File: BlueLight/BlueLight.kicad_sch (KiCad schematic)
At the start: 9 parts, among them J1 Rotary Encoder, J2 LED, SW1 SW_Push_Dual, SW2 SW_Push_Dual, SW3 SW_Push_Dual

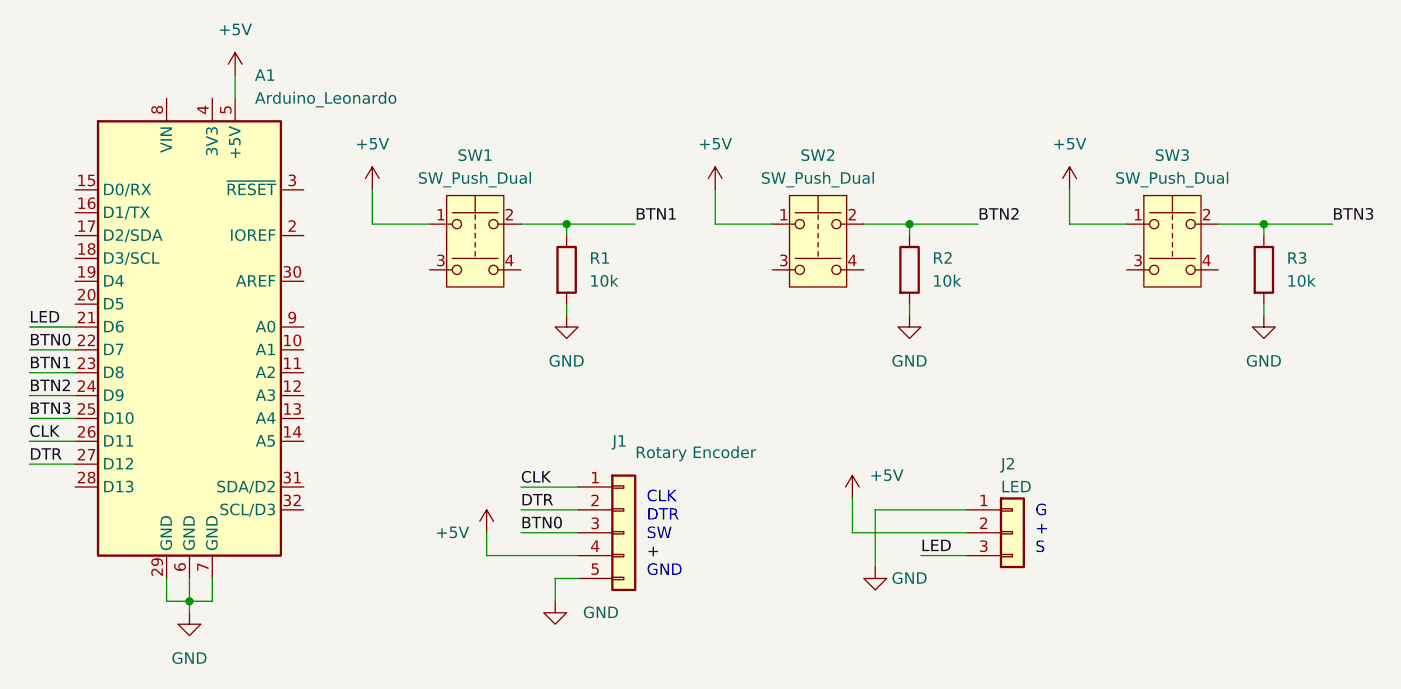
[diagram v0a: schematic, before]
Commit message: new app
timer added
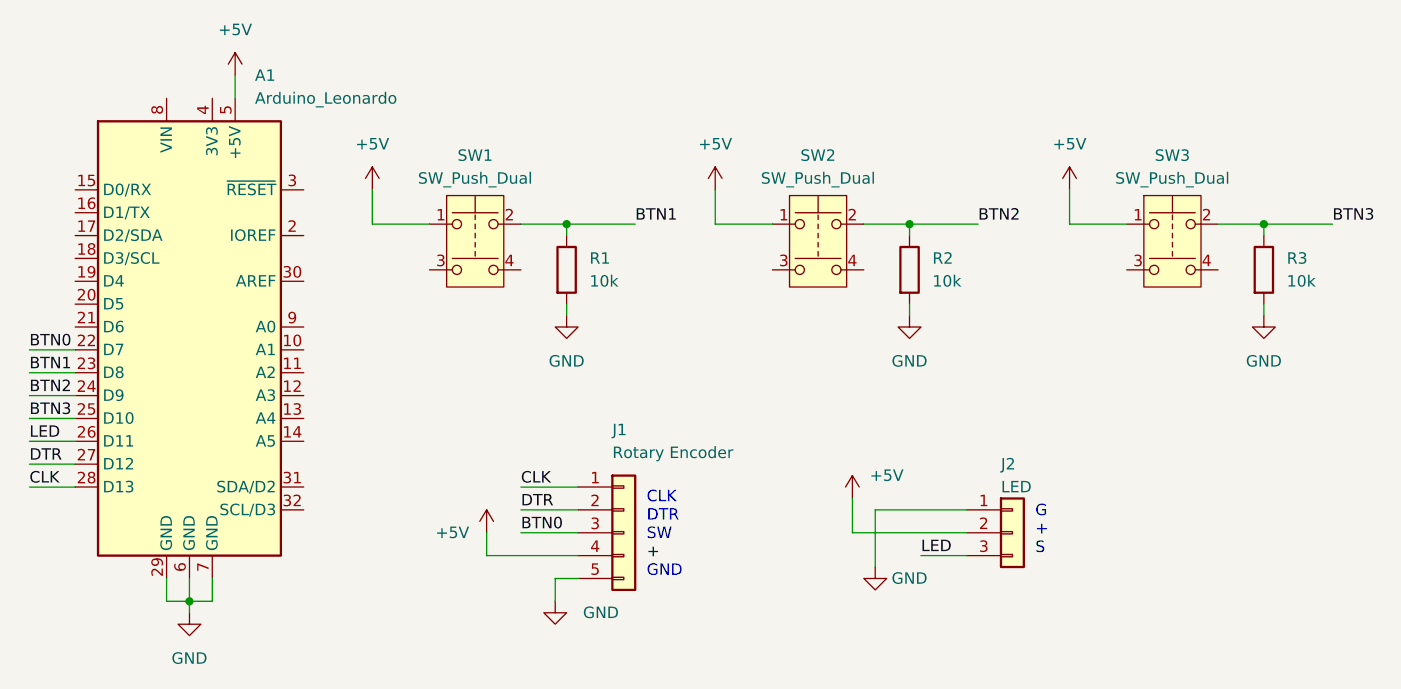
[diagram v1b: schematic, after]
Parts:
- A1: footprint Module:Arduino_UNO_R3 -> Module:Arduino_UNO_R3_WithMountingHoles
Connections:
- net CLK: now also A1.28 (D13); no longer A1.26 (D11)
- net LED: now also A1.26 (D11); no longer A1.21 (D6)
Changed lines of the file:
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@@
+    (stroke (width 0) (type default))
+  )
+  (wire (pts (xy 17.78 69.85) (xy 22.86 69.85))
     (stroke (width 0) (type default))
   )
@@
     (stroke (width 0) (type default))
   )
-  (wire (pts (xy 17.78 52.07) (xy 22.86 52.07))
-    (stroke (width 0) (type default))
-  )
   (wire (pts (xy 77.47 49.53) (xy 77.47 50.8))
     (stroke (width 0) (type default))
@@
     (effects (font (size 1.27 1.27)) (justify left bottom))
   )
-  (label "CLK" (at 17.78 64.77 0) (fields_autoplaced)
+  (label "CLK" (at 17.78 69.85 0) (fields_autoplaced)
     (effects (font (size 1.27 1.27)) (justify left bottom))
   )
@@
     (effects (font (size 1.27 1.27)) (justify left bottom))
   )
-  (label "LED" (at 17.78 52.07 0) (fields_autoplaced)
+  (label "LED" (at 17.78 64.77 0) (fields_autoplaced)
     (effects (font (size 1.27 1.27)) (justify left bottom))
   )
@@
   (symbol (lib_id "Connector_Generic:Conn_01x05") (at 83.82 74.93 0) (unit 1)
     (in_bom yes) (on_board yes) (dnp no)
-    (property "Reference" "J1" (at 82.55 64.77 0)
-      (effects (font (size 1.27 1.27)) (justify left))
-    )
-    (property "Value" "Rotary Encoder" (at 85.09 66.04 0)
+    (property "Reference" "J1" (at 82.55 63.5 0)
+      (effects (font (size 1.27 1.27)) (justify left))
+    )
+    (property "Value" "Rotary Encoder" (at 82.55 66.04 0)
       (effects (font (size 1.27 1.27)) (justify left))
     )
@@
       (effects (font (size 1.27 1.27)) (justify left))
     )
-    (property "Footprint" "Module:Arduino_UNO_R3" (at 35.56 52.07 0)
+    (property "Footprint" "Module:Arduino_UNO_R3_WithMountingHoles" (at 35.56 52.07 0)
       (effects (font (size 1.27 1.27) italic) hide)
     )

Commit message: doule version init
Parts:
- added J3: LED, Connector_PinHeader_2.54mm:PinHeader_1x03_P2.54mm_Vertical, symbol Connector_Generic:Conn_01x03
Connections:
- net +5V: now also J3.2 (Pin_2)
- net GND: now also J3.1 (Pin_1)
- net LED_2: now reaches A1.18 (D3/SCL)
- net LED_2: now also J3.3 (Pin_3)
- net LED renamed LED_1
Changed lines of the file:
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@@
+    (stroke (width 0) (type default))
+  )
+  (wire (pts (xy 144.78 71.12) (xy 144.78 74.93))
     (stroke (width 0) (type default))
   )
@@
     (stroke (width 0) (type default))
   )
-  (wire (pts (xy 17.78 57.15) (xy 22.86 57.15))
+  (wire (pts (xy 16.51 57.15) (xy 22.86 57.15))
     (stroke (width 0) (type default))
   )
@@
     (stroke (width 0) (type default))
   )
-  (wire (pts (xy 17.78 64.77) (xy 22.86 64.77))
+  (wire (pts (xy 16.51 64.77) (xy 22.86 64.77))
     (stroke (width 0) (type default))
   )
@@
     (stroke (width 0) (type default))
   )
+  (wire (pts (xy 16.51 44.45) (xy 22.86 44.45))
+    (stroke (width 0) (type default))
+  )
   (wire (pts (xy 115.57 40.64) (xy 123.19 40.64))
     (stroke (width 0) (type default))
   )
-  (wire (pts (xy 17.78 67.31) (xy 22.86 67.31))
+  (wire (pts (xy 16.51 67.31) (xy 22.86 67.31))
     (stroke (width 0) (type default))
   )
@@
     (stroke (width 0) (type default))
   )
-  (wire (pts (xy 17.78 69.85) (xy 22.86 69.85))
+  (wire (pts (xy 16.51 54.61) (xy 22.86 54.61))
+    (stroke (width 0) (type default))
+  )
+  (wire (pts (xy 16.51 69.85) (xy 22.86 69.85))
     (stroke (width 0) (type default))
   )
@@
     (stroke (width 0) (type default))
   )
-  (wire (pts (xy 17.78 62.23) (xy 22.86 62.23))
-    (stroke (width 0) (type default))
-  )
   (wire (pts (xy 35.56 80.01) (xy 35.56 82.55))
     (stroke (width 0) (type default))
@@
     (stroke (width 0) (type default))
   )
+  (wire (pts (xy 152.4 77.47) (xy 157.48 77.47))
+    (stroke (width 0) (type default))
+  )
+  (wire (pts (xy 147.32 72.39) (xy 147.32 78.74))
+    (stroke (width 0) (type default))
+  )
   (wire (pts (xy 111.76 72.39) (xy 111.76 78.74))
     (stroke (width 0) (type default))
@@
     (stroke (width 0) (type default))
   )
+  (wire (pts (xy 147.32 72.39) (xy 157.48 72.39))
+    (stroke (width 0) (type default))
+  )
   (wire (pts (xy 77.47 49.53) (xy 77.47 50.8))
     (stroke (width 0) (type default))
   )
+  (wire (pts (xy 16.51 59.69) (xy 22.86 59.69))
+    (stroke (width 0) (type default))
+  )
+  (wire (pts (xy 16.51 62.23) (xy 22.86 62.23))
+    (stroke (width 0) (type default))
+  )
   (wire (pts (xy 111.76 72.39) (xy 121.92 72.39))
     (stroke (width 0) (type default))
   )
-  (wire (pts (xy 17.78 59.69) (xy 22.86 59.69))
-    (stroke (width 0) (type default))
-  )
   (wire (pts (xy 154.94 40.64) (xy 162.56 40.64))
     (stroke (width 0) (type default))
@@
     (stroke (width 0) (type default))
   )
-  (wire (pts (xy 17.78 54.61) (xy 22.86 54.61))
-    (stroke (width 0) (type default))
-  )
   (wire (pts (xy 38.1 82.55) (xy 38.1 80.01))
     (stroke (width 0) (type default))
   )
+  (wire (pts (xy 144.78 74.93) (xy 157.48 74.93))
+    (stroke (width 0) (type default))
+  )
+  (text "G\n+\nS" (at 165.1 77.47 0)
+    (effects (font (size 1.27 1.27)) (justify left bottom))
+  )
   (text "G\n+\nS" (at 129.54 77.47 0)
     (effects (font (size 1.27 1.27)) (justify left bottom))
@@
     (effects (font (size 1.27 1.27)) (justify left bottom))
   )
-  (label "DTR" (at 17.78 67.31 0) (fields_autoplaced)
-    (effects (font (size 1.27 1.27)) (justify left bottom))
-  )
-  (label "CLK" (at 17.78 69.85 0) (fields_autoplaced)
+  (label "DTR" (at 16.51 67.31 0) (fields_autoplaced)
+    (effects (font (size 1.27 1.27)) (justify left bottom))
+  )
+  (label "CLK" (at 16.51 69.85 0) (fields_autoplaced)
     (effects (font (size 1.27 1.27)) (justify left bottom))
   )
@@
     (effects (font (size 1.27 1.27)) (justify left bottom))
   )
-  (label "BTN2" (at 17.78 59.69 0) (fields_autoplaced)
-    (effects (font (size 1.27 1.27)) (justify left bottom))
-  )
-  (label "LED" (at 116.84 77.47 0) (fields_autoplaced)
+  (label "BTN2" (at 16.51 59.69 0) (fields_autoplaced)
+    (effects (font (size 1.27 1.27)) (justify left bottom))
+  )
+  (label "LED_1" (at 116.84 77.47 0) (fields_autoplaced)
     (effects (font (size 1.27 1.27)) (justify left bottom))
   )
@@
     (effects (font (size 1.27 1.27)) (justify left bottom))
   )
-  (label "BTN3" (at 17.78 62.23 0) (fields_autoplaced)
+  (label "LED_2" (at 16.51 44.45 0) (fields_autoplaced)
+    (effects (font (size 1.27 1.27)) (justify left bottom))
+  )
+  (label "BTN3" (at 16.51 62.23 0) (fields_autoplaced)
+    (effects (font (size 1.27 1.27)) (justify left bottom))
+  )
+  (label "LED_2" (at 152.4 77.47 0) (fields_autoplaced)
     (effects (font (size 1.27 1.27)) (justify left bottom))
   )
@@
     (effects (font (size 1.27 1.27)) (justify left bottom))
   )
-  (label "BTN1" (at 17.78 57.15 0) (fields_autoplaced)
-    (effects (font (size 1.27 1.27)) (justify left bottom))
-  )
-  (label "LED" (at 17.78 64.77 0) (fields_autoplaced)
+  (label "BTN1" (at 16.51 57.15 0) (fields_autoplaced)
+    (effects (font (size 1.27 1.27)) (justify left bottom))
+  )
+  (label "LED_1" (at 16.51 64.77 0) (fields_autoplaced)
     (effects (font (size 1.27 1.27)) (justify left bottom))
   )
@@
     (effects (font (size 1.27 1.27)) (justify left bottom))
   )
-  (label "BTN0" (at 17.78 54.61 0) (fields_autoplaced)
+  (label "BTN0" (at 16.51 54.61 0) (fields_autoplaced)
     (effects (font (size 1.27 1.27)) (justify left bottom))
   )
@@
     )
   )
+  (symbol (lib_id "power:GND") (at 147.32 78.74 0) (unit 1)
+    (in_bom yes) (on_board yes) (dnp no)
+    (property "Reference" "#PWR014" (at 147.32 85.09 0)
+      (effects (font (size 1.27 1.27)) hide)
+    )
+    (property "Value" "GND" (at 151.13 80.01 0)
+      (effects (font (size 1.27 1.27)))
+    )
+    (property "Footprint" "" (at 147.32 78.74 0)
+      (effects (font (size 1.27 1.27)) hide)
+    )
+    (property "Datasheet" "" (at 147.32 78.74 0)
+      (effects (font (size 1.27 1.27)) hide)
+    )
+    (pin "1")
+    (instances
+      (project "BlueLight"
+        (path "/fdf44142-1775-4060-9889-258aa675e066"
+          (reference "#PWR014") (unit 1)
+        )
+      )
+    )
+  )
   (symbol (lib_id "power:GND") (at 154.94 50.8 0) (unit 1)
     (in_bom yes) (on_board yes) (dnp no) (fields_autoplaced)
@@
         )
       )
+    )
+  )
+  (symbol (lib_id "Connector_Generic:Conn_01x03") (at 162.56 74.93 0) (unit 1)
+    (in_bom yes) (on_board yes) (dnp no)
+    (property "Reference" "J3" (at 161.29 67.31 0)
+      (effects (font (size 1.27 1.27)) (justify left))
+    )
+    (property "Value" "LED" (at 161.29 69.85 0)
+      (effects (font (size 1.27 1.27)) (justify left))
+    )
+    (property "Footprint" "Connector_PinHeader_2.54mm:PinHeader_1x03_P2.54mm_Vertical" (at 162.56 74.93 0)
+      (effects (font (size 1.27 1.27)) hide)
+    )
+    (property "Datasheet" "~" (at 162.56 74.93 0)
+      (effects (font (size 1.27 1.27)) hide)
+    )
+    (pin "3")
+    (pin "1")
+    (pin "2")
+    (instances
+      (project "BlueLight"
+        (path "/fdf44142-1775-4060-9889-258aa675e066"
+          (reference "J3") (unit 1)
+        )
+      )
+    )
+  )
+  (symbol (lib_id "power:+5V") (at 144.78 71.12 0) (unit 1)
+    (in_bom yes) (on_board yes) (dnp no)
+    (property "Reference" "#PWR013" (at 144.78 74.93 0)
+      (effects (font (size 1.27 1.27)) hide)
+    )
+    (property "Value" "+5V" (at 148.59 68.58 0)
+      (effects (font (size 1.27 1.27)))
+    )
+    (property "Footprint" "" (at 144.78 71.12 0)
+      (effects (font (size 1.27 1.27)) hide)
+    )
+    (property "Datasheet" "" (at 144.78 71.12 0)
+      (effects (font (size 1.27 1.27)) hide)
+    )
+    (pin "1")
+    (instances
+      (project "BlueLight"
+        (path "/fdf44142-1775-4060-9889-258aa675e066"
+          (reference "#PWR013") (unit 1)
+        )
+      )
